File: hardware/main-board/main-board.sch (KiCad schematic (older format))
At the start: 31 parts, among them J2 STDC14, J3 NHD OLED Connector, U4 STM32F411RETx, U5 PAM8904EJP, U6 M24M01-RMN, Y1 16MHz

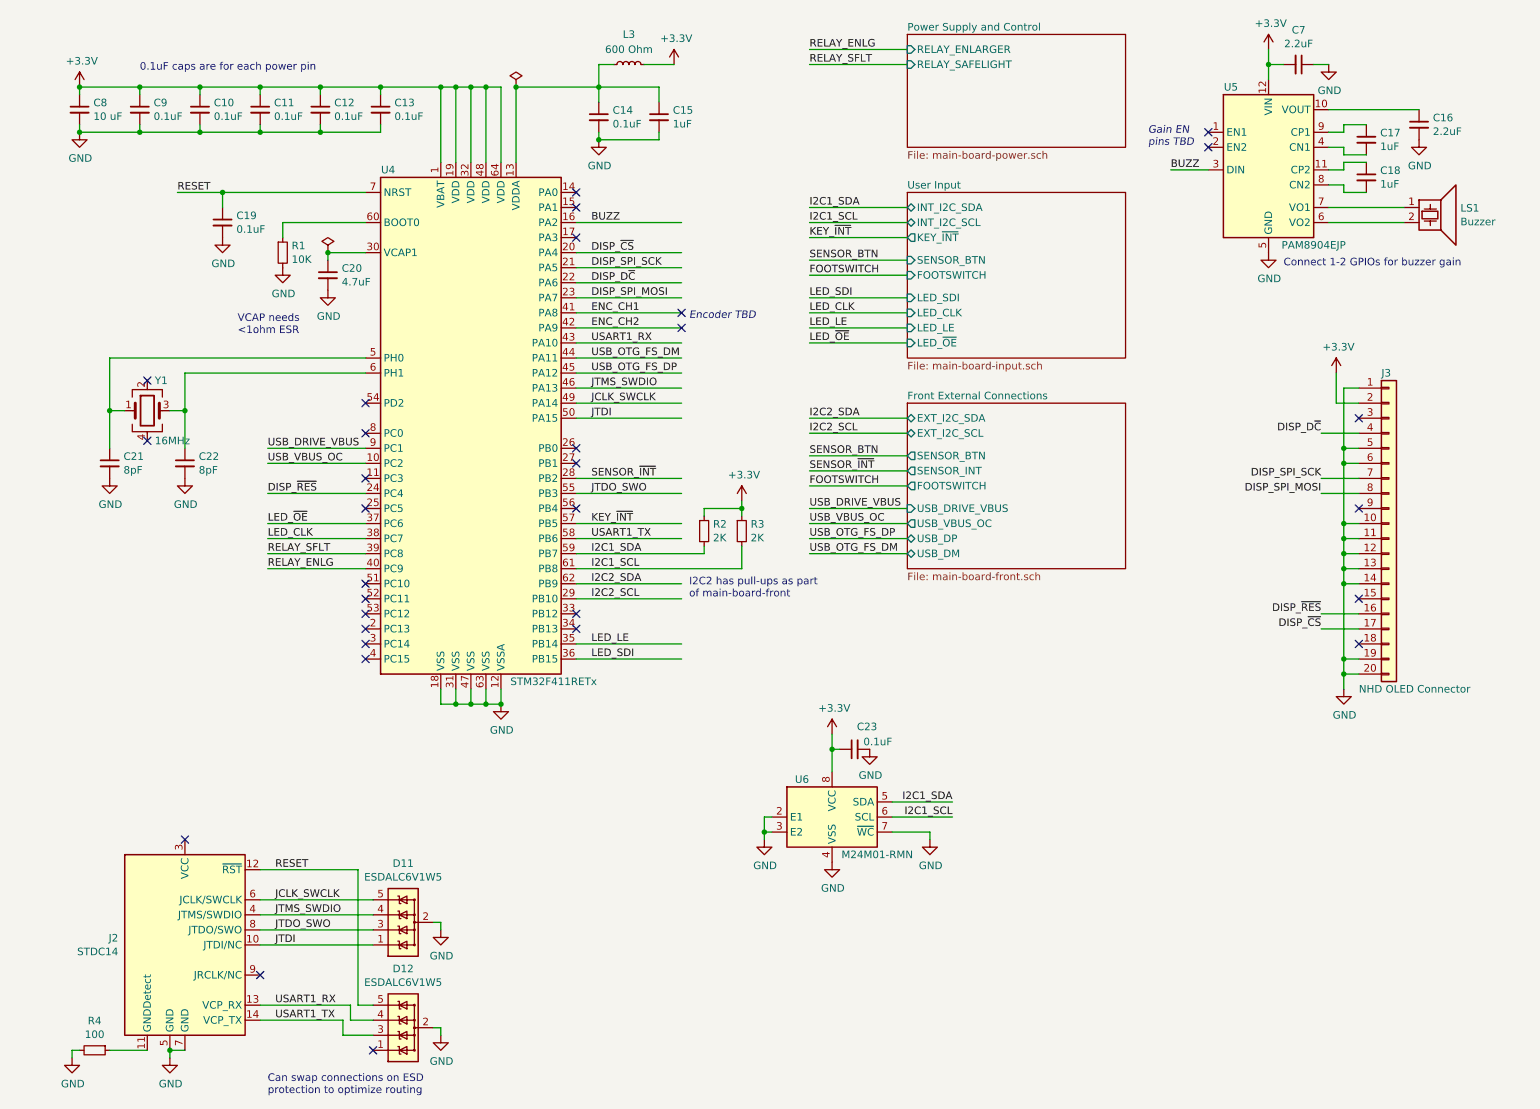
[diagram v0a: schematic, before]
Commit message: Fill in BOM data for all known components
Added BOM assignments for main board components
Fixed GNDDetect connection on STDC14 connector

Added more notes to the main board schematic of things that are still
TBD or need fixing.
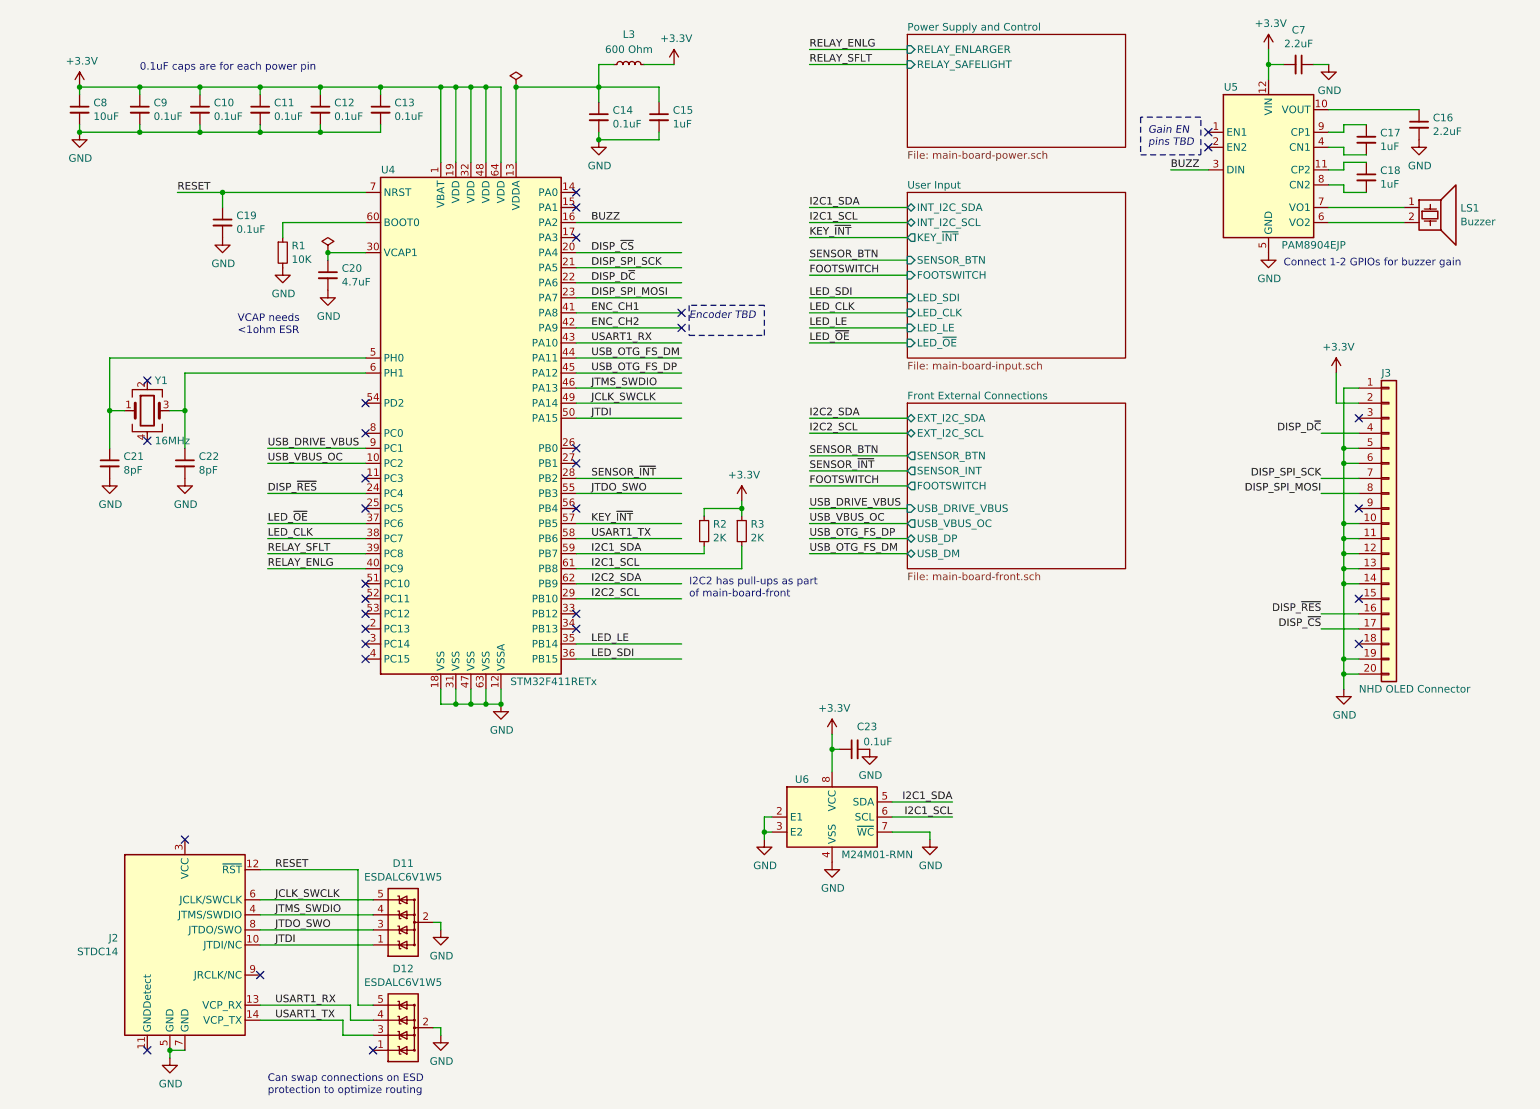
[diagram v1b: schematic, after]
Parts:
- removed R4: 100, symbol Device:R_Small
- C10, C11, C12, C13, C14, C19, C23, C9: footprint (none) -> Capacitor_SMD:C_0603_1608Metric; Description (none) -> CAP CER 0.1UF 25V X7R 0603; Manufacturer (none) -> Samsung Electro-Mechanics; Manufacturer PN (none) -> CL10B104KA8NNNC; Supplier (none) -> Digi-Key; Supplier PN (none) -> 1276-1006-1-ND
- C15: footprint (none) -> Capacitor_SMD:C_0603_1608Metric; Description (none) -> CAP CER 1UF 25V X7R 0603; Manufacturer (none) -> Samsung Electro-Mechanics; Manufacturer PN (none) -> CL10B105KA8NNNC; Supplier (none) -> Digi-Key; Supplier PN (none) -> 1276-1184-1-ND
- C21, C22: footprint (none) -> Capacitor_SMD:C_0603_1608Metric; Description (none) -> CAP CER 8PF 50V NPO 0603; Manufacturer (none) -> Yageo; Manufacturer PN (none) -> CC0603CRNPO9BN8R0; Supplier (none) -> Digi-Key; Supplier PN (none) -> 311-3864-1-ND
- C8: value 10 uF -> 10uF; footprint (none) -> Capacitor_SMD:C_0805_2012Metric; Description (none) -> CAP CER 10UF 25V X5R 0805; Manufacturer (none) -> Samsung Electro-Mechanics; Manufacturer PN (none) -> CL21A106KAYNNNG; Supplier (none) -> Digi-Key; Supplier PN (none) -> 1276-6454-1-ND
- D11, D12: Description (none) -> TVS DIODE 3V SOT323-5; Manufacturer (none) -> STMicroelectronics; Manufacturer PN (none) -> ESDALC6V1W5; Supplier (none) -> Digi-Key; Supplier PN (none) -> 497-7231-1-ND
- J2: Description (none) -> CONN HEADER SMD 14POS 1.27MM; Manufacturer (none) -> Samtec Inc.; Manufacturer PN (none) -> FTSH-107-01-L-DV-K-A; Supplier (none) -> Mouser; Supplier PN (none) -> 200-FTSH10701LDVKA
- J3: Description (none) -> CONN HDR 20POS 0.1 GOLD PCB; Manufacturer (none) -> Sullins Connector Solutions; Manufacturer PN (none) -> PPPC201LFBN-RC; Supplier (none) -> Digi-Key; Supplier PN (none) -> PPPC201LFBN-RC
- R1: footprint (none) -> Resistor_SMD:R_0603_1608Metric; Description (none) -> RES SMD 10K OHM 5% 1/10W 0603; Manufacturer (none) -> Vishay Dale; Manufacturer PN (none) -> CRCW060310K0JNEA; Supplier (none) -> Digi-Key; Supplier PN (none) -> 541-10KGCT-ND
- R2, R3: footprint (none) -> Resistor_SMD:R_0603_1608Metric; Description (none) -> RES SMD 2K OHM 5% 1/10W 0603; Manufacturer (none) -> Vishay Dale; Manufacturer PN (none) -> CRCW06032K00JNEA; Supplier (none) -> Digi-Key; Supplier PN (none) -> 541-2.0KGCT-ND
- U4: Description (none) -> IC MCU 32BIT 512KB FLASH 64LQFP; Manufacturer (none) -> STMicroelectronics; Manufacturer PN (none) -> STM32F411RET6; Supplier (none) -> Digi-Key; Supplier PN (none) -> 497-14909-ND
- U6: Description (none) -> IC EEPROM 1M I2C 1MHZ 8SO; Manufacturer (none) -> STMicroelectronics; Manufacturer PN (none) -> M24M01-RMN6TP; Supplier (none) -> Digi-Key; Supplier PN (none) -> 497-6351-1-ND
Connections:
- wire segments 203 -> 200
- no-connect marks 31 -> 32

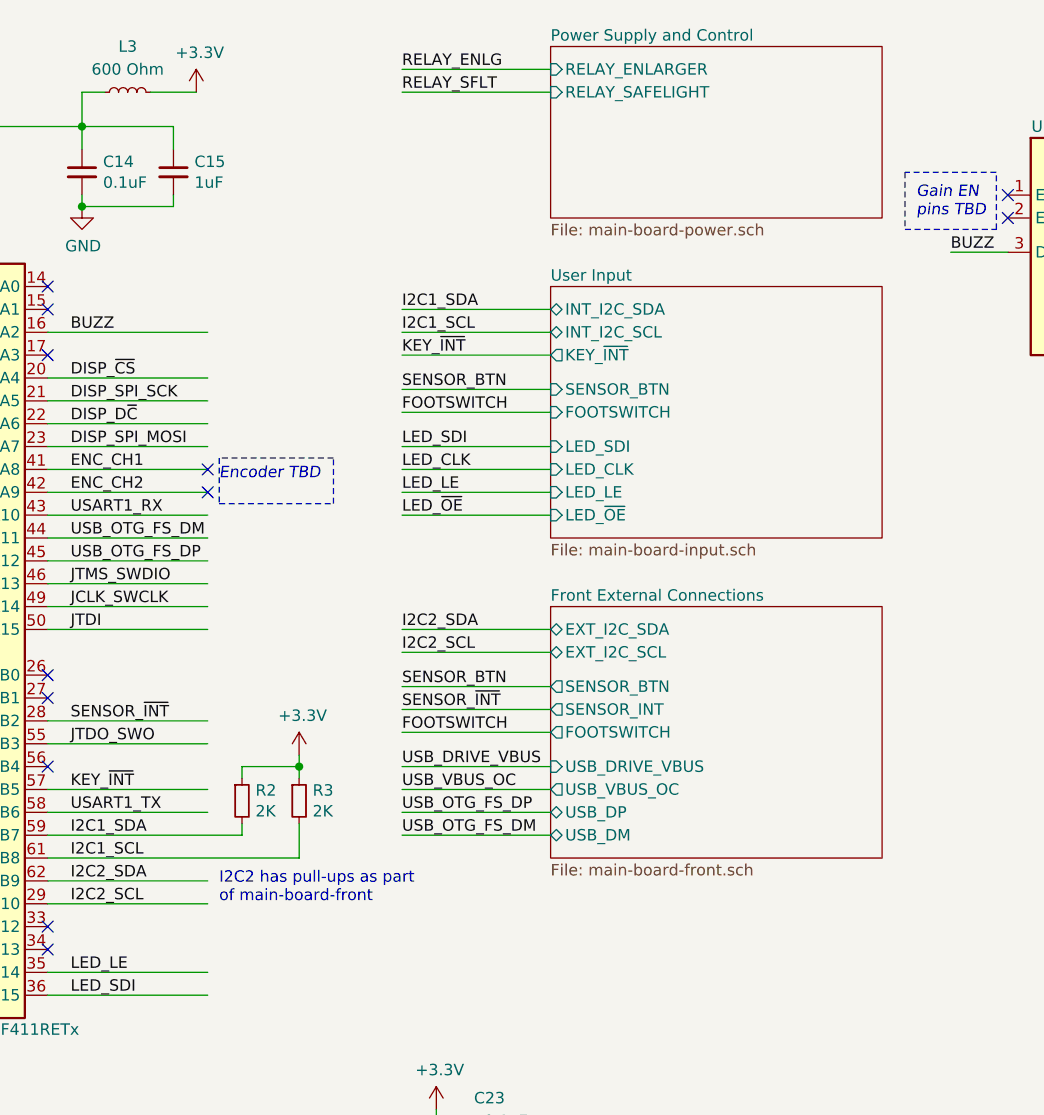
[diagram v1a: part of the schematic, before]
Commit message: Added rotary encoder
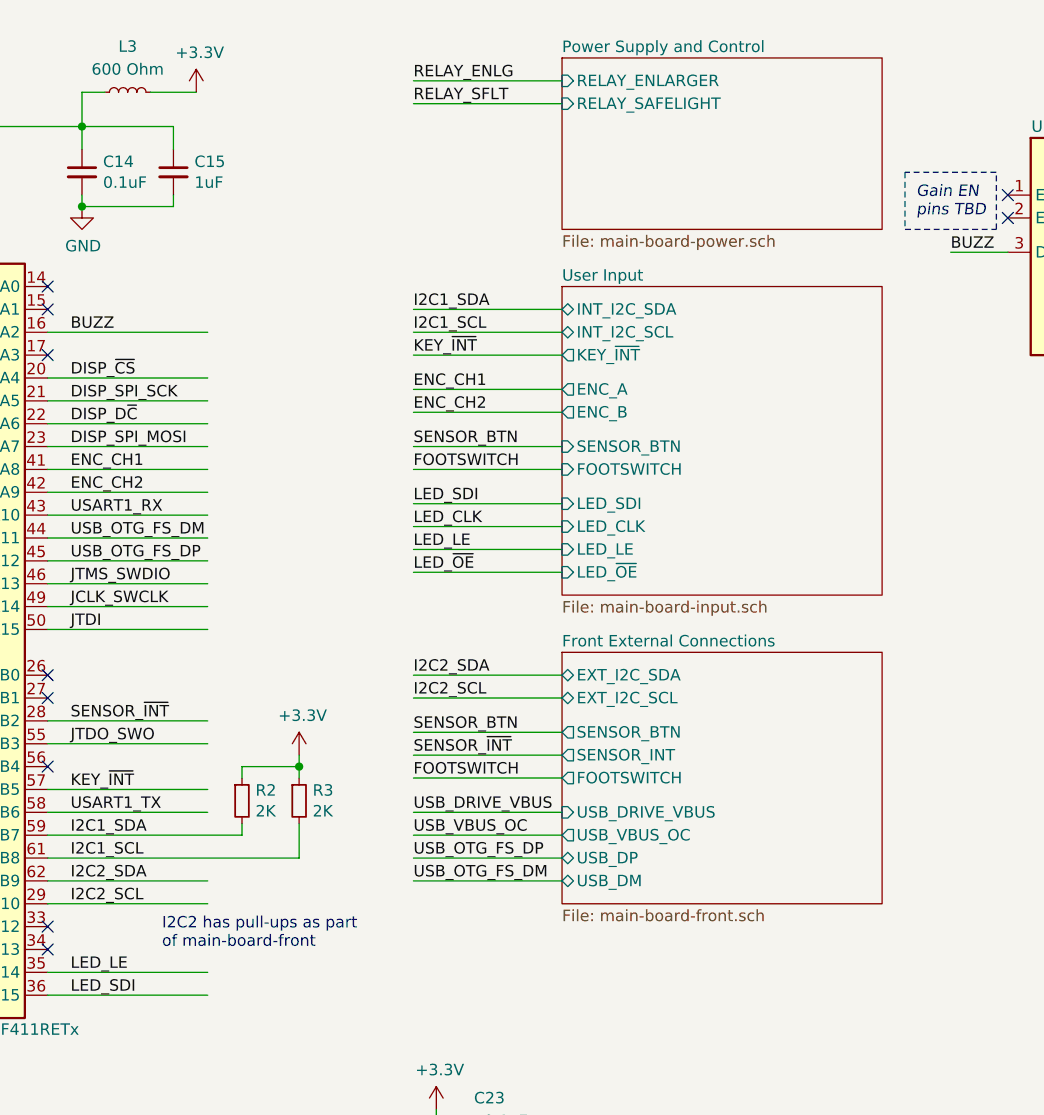
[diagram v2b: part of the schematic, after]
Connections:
- wire segments 200 -> 202
- no-connect marks 32 -> 30
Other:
- note removed: "Encoder TBD"
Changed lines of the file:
@@
 $EndComp
 $Sheet
-S 6500 700  1450 750
+S 6550 750  1400 750
 U 5F8B674D
 F0 "Power Supply and Control" 50
 F1 "main-board-power.sch" 50
-F2 "RELAY_ENLARGER" I L 6500 800 50
-F3 "RELAY_SAFELIGHT" I L 6500 900 50
+F2 "RELAY_ENLARGER" I L 6550 850 50
+F3 "RELAY_SAFELIGHT" I L 6550 950 50
 $EndSheet
 $Sheet
-S 6500 1750 1450 1100
+S 6550 1750 1400 1350
 U 5F8B69B5
 F0 "User Input" 50
 F1 "main-board-input.sch" 50
-F2 "INT_I2C_SDA" B L 6500 1850 50
-F3 "INT_I2C_SCL" B L 6500 1950 50
-F4 "SENSOR_BTN" I L 6500 2200 50
-F5 "FOOTSWITCH" I L 6500 2300 50
-F6 "LED_SDI" I L 6500 2450 50
-F7 "LED_CLK" I L 6500 2550 50
-F8 "LED_LE" I L 6500 2650 50
-F9 "LED_~OE" I L 6500 2750 50
-F10 "KEY_~INT" O L 6500 2050 50
+F2 "INT_I2C_SDA" B L 6550 1850 50
+F3 "INT_I2C_SCL" B L 6550 1950 50
+F4 "SENSOR_BTN" I L 6550 2450 50
+F5 "FOOTSWITCH" I L 6550 2550 50
+F6 "LED_SDI" I L 6550 2700 50
+F7 "LED_CLK" I L 6550 2800 50
+F8 "LED_LE" I L 6550 2900 50
+F9 "LED_~OE" I L 6550 3000 50
+F10 "KEY_~INT" O L 6550 2050 50
+F11 "ENC_A" O L 6550 2200 50
+F12 "ENC_B" O L 6550 2300 50
 $EndSheet
 $Comp
@@
 Text Label 9250 4650 2    50   ~ 0
 DISP_~CS
-$Sheet
-S 6500 3150 1450 1100
-U 5FA19AFF
-F0 "Front External Connections" 50
-F1 "main-board-front.sch" 50
-F2 "EXT_I2C_SDA" B L 6500 3250 50
-F3 "EXT_I2C_SCL" B L 6500 3350 50
-F4 "SENSOR_BTN" O L 6500 3500 50
-F5 "SENSOR_INT" O L 6500 3600 50
-F6 "FOOTSWITCH" O L 6500 3700 50
-F7 "USB_DRIVE_VBUS" I L 6500 3850 50
-F8 "USB_VBUS_OC" O L 6500 3950 50
-F9 "USB_DP" B L 6500 4050 50
-F10 "USB_DM" B L 6500 4150 50
-$EndSheet
 $Comp
 L Project:Conn_ST_STDC14 J2
@@
 Can swap connections on ESD\nprotection to optimize routing
 NoConn ~ 1700 6050
-Text Label 5850 3350 0    50   ~ 0
+Text Label 5900 3550 0    50   ~ 0
 I2C2_SCL
-Text Label 5850 3250 0    50   ~ 0
+Text Label 5900 3450 0    50   ~ 0
 I2C2_SDA
-Text Label 5850 3600 0    50   ~ 0
+Text Label 5900 3800 0    50   ~ 0
 SENSOR_~INT
-Text Label 5850 4150 0    50   ~ 0
+Text Label 5900 4350 0    50   ~ 0
 USB_OTG_FS_DM
-Text Label 5850 4050 0    50   ~ 0
+Text Label 5900 4250 0    50   ~ 0
 USB_OTG_FS_DP
-Text Label 5850 3850 0    50   ~ 0
+Text Label 5900 4050 0    50   ~ 0
 USB_DRIVE_VBUS
-Text Label 5850 3950 0    50   ~ 0
+Text Label 5900 4150 0    50   ~ 0
 USB_VBUS_OC
-Wire Wire Line
-	6500 3250 5850 3250
-Wire Wire Line
-	5850 3350 6500 3350
-Wire Wire Line
-	5850 3600 6500 3600
-Wire Wire Line
-	6500 3850 5850 3850
-Wire Wire Line
-	5850 3950 6500 3950
-Wire Wire Line
-	5850 4050 6500 4050
-Wire Wire Line
-	5850 4150 6500 4150
-Text Label 5850 2200 0    50   ~ 0
+Text Label 5900 2450 0    50   ~ 0
 SENSOR_BTN
-Text Label 5850 2300 0    50   ~ 0
+Text Label 5900 2550 0    50   ~ 0
 FOOTSWITCH
-Text Label 5850 3500 0    50   ~ 0
+Text Label 5900 3700 0    50   ~ 0
 SENSOR_BTN
-Text Label 5850 3700 0    50   ~ 0
+Text Label 5900 3900 0    50   ~ 0
 FOOTSWITCH
 Wire Wire Line
-	6500 2200 5850 2200
-Wire Wire Line
-	5850 2300 6500 2300
-Wire Wire Line
-	5850 3700 6500 3700
-Wire Wire Line
-	5850 3500 6500 3500
-Text Label 5850 1850 0    50   ~ 0
+	6550 2450 5900 2450
+Wire Wire Line
+	5900 2550 6550 2550
+Text Label 5900 1850 0    50   ~ 0
 I2C1_SDA
-Text Label 5850 1950 0    50   ~ 0
+Text Label 5900 1950 0    50   ~ 0
 I2C1_SCL
 Wire Wire Line
-	5850 1950 6500 1950
-Wire Wire Line
-	5850 1850 6500 1850
-Text Label 5850 2050 0    50   ~ 0
+	5900 1950 6550 1950
+Wire Wire Line
+	5900 1850 6550 1850
+Text Label 5900 2050 0    50   ~ 0
 KEY_~INT
 Wire Wire Line
-	5850 2050 6500 2050
-Text Notes 5050 4450 0    50   ~ 0
+	5900 2050 6550 2050
+Text Notes 4800 4650 0    50   ~ 0
 I2C2 has pull-ups as part\nof main-board-front
-Text Label 5850 900  0    50   ~ 0
+Text Label 5900 950  0    50   ~ 0
 RELAY_SFLT
-Text Label 5850 800  0    50   ~ 0
+Text Label 5900 850  0    50   ~ 0
 RELAY_ENLG
 Wire Wire Line
-	6500 800  5850 800
-Wire Wire Line
-	6500 900  5850 900
+	6550 850  5900 850
+Wire Wire Line
+	6550 950  5900 950
 Text Label 2250 4150 0    50   ~ 0
 RELAY_SFLT
@@
 Wire Wire Line
 	4300 4850 5000 4850
-Text Label 5850 2750 0    50   ~ 0
+Text Label 5900 3000 0    50   ~ 0
 LED_~OE
-Text Label 5850 2550 0    50   ~ 0
+Text Label 5900 2800 0    50   ~ 0
 LED_CLK
-Text Label 5850 2650 0    50   ~ 0
+Text Label 5900 2900 0    50   ~ 0
 LED_LE
-Text Label 5850 2450 0    50   ~ 0
+Text Label 5900 2700 0    50   ~ 0
 LED_SDI
 Wire Wire Line
-	6500 2450 5850 2450
-Wire Wire Line
-	6500 2550 5850 2550
-Wire Wire Line
-	6500 2650 5850 2650
-Wire Wire Line
-	6500 2750 5850 2750
+	6550 2700 5900 2700
+Wire Wire Line
+	6550 2800 5900 2800
+Wire Wire Line
+	6550 2900 5900 2900
+Wire Wire Line
+	6550 3000 5900 3000
 NoConn ~ 4300 1750
 NoConn ~ 4300 1850
@@
 Text Notes 8100 1450 0    50   Italic 0
 Gain EN\npins TBD
-NoConn ~ 5000 2550
-NoConn ~ 5000 2650
-Text Notes 5050 2600 0    50   Italic 0
-Encoder TBD
 $Comp
 L power:PWR_FLAG #FLG0108
@@
 $EndComp
 Connection ~ 2650 2150
-Wire Notes Line
-	5050 2500 5050 2700
-Wire Notes Line
-	5050 2700 5550 2700
-Wire Notes Line
-	5550 2700 5550 2500
-Wire Notes Line
-	5550 2500 5050 2500
 Wire Notes Line
 	8450 1500 8450 1250
@@
 	8050 1500 8450 1500
 NoConn ~ 1450 7450
+Wire Wire Line
+	5900 4350 6550 4350
+Wire Wire Line
+	5900 4250 6550 4250
+Wire Wire Line
+	5900 4150 6550 4150
+Wire Wire Line
+	6550 4050 5900 4050
+Wire Wire Line
+	5900 3900 6550 3900
+Wire Wire Line
+	5900 3800 6550 3800
+Wire Wire Line
+	5900 3700 6550 3700
+Wire Wire Line
+	5900 3550 6550 3550
+Wire Wire Line
+	6550 3450 5900 3450
+$Sheet
+S 6550 3350 1400 1100
+U 5FA19AFF
+F0 "Front External Connections" 50
+F1 "main-board-front.sch" 50
+F2 "EXT_I2C_SDA" B L 6550 3450 50
+F3 "EXT_I2C_SCL" B L 6550 3550 50
+F4 "SENSOR_BTN" O L 6550 3700 50
+F5 "SENSOR_INT" O L 6550 3800 50
+F6 "FOOTSWITCH" O L 6550 3900 50
+F7 "USB_DRIVE_VBUS" I L 6550 4050 50
+F8 "USB_VBUS_OC" O L 6550 4150 50
+F9 "USB_DP" B L 6550 4250 50
+F10 "USB_DM" B L 6550 4350 50
+$EndSheet
+Text Label 5900 2200 0    50   ~ 0
+ENC_CH1
+Text Label 5900 2300 0    50   ~ 0
+ENC_CH2
+Wire Wire Line
+	5900 2200 6550 2200
+Wire Wire Line
+	5900 2300 6550 2300
 $EndSCHEMATC
